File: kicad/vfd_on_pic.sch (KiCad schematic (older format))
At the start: 8 parts, among them J1 ICSP Header, J2 I2C and Power, J3 Elements, J4 Grid Multiplexor, U1 PIC16F18345

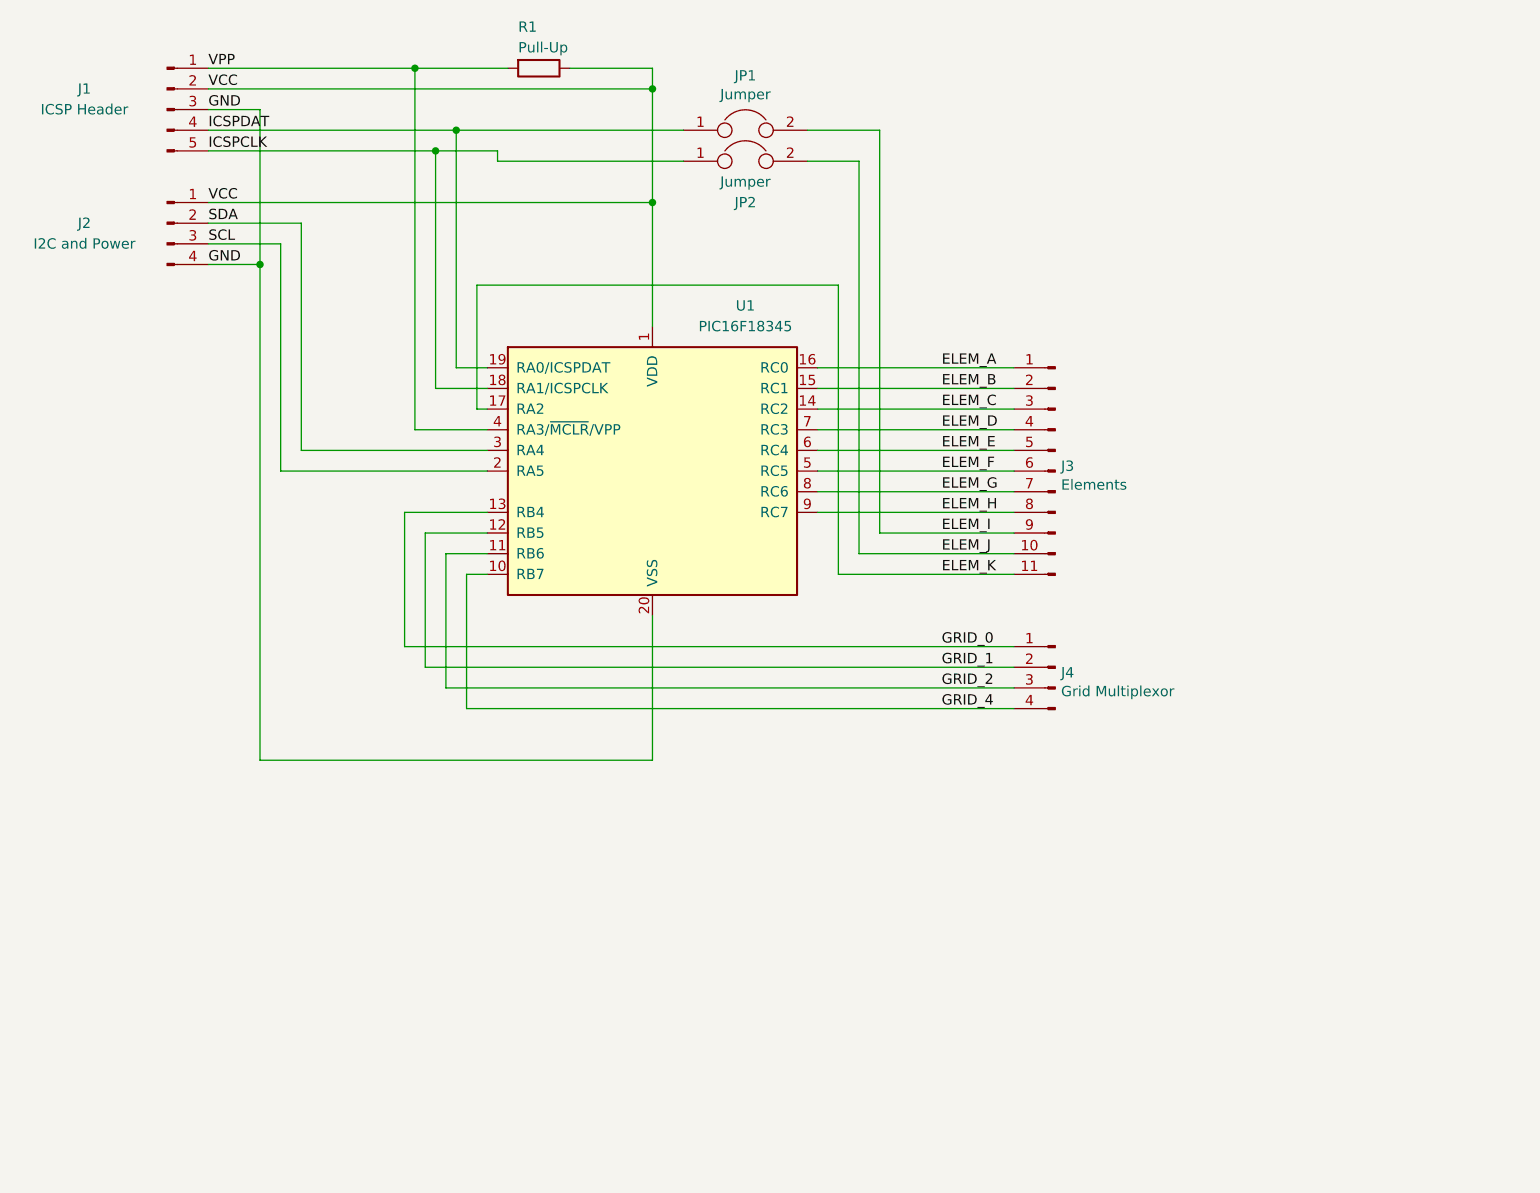
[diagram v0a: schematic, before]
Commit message: Add 74x138 3-8 decoder and uln2003 Darlington array
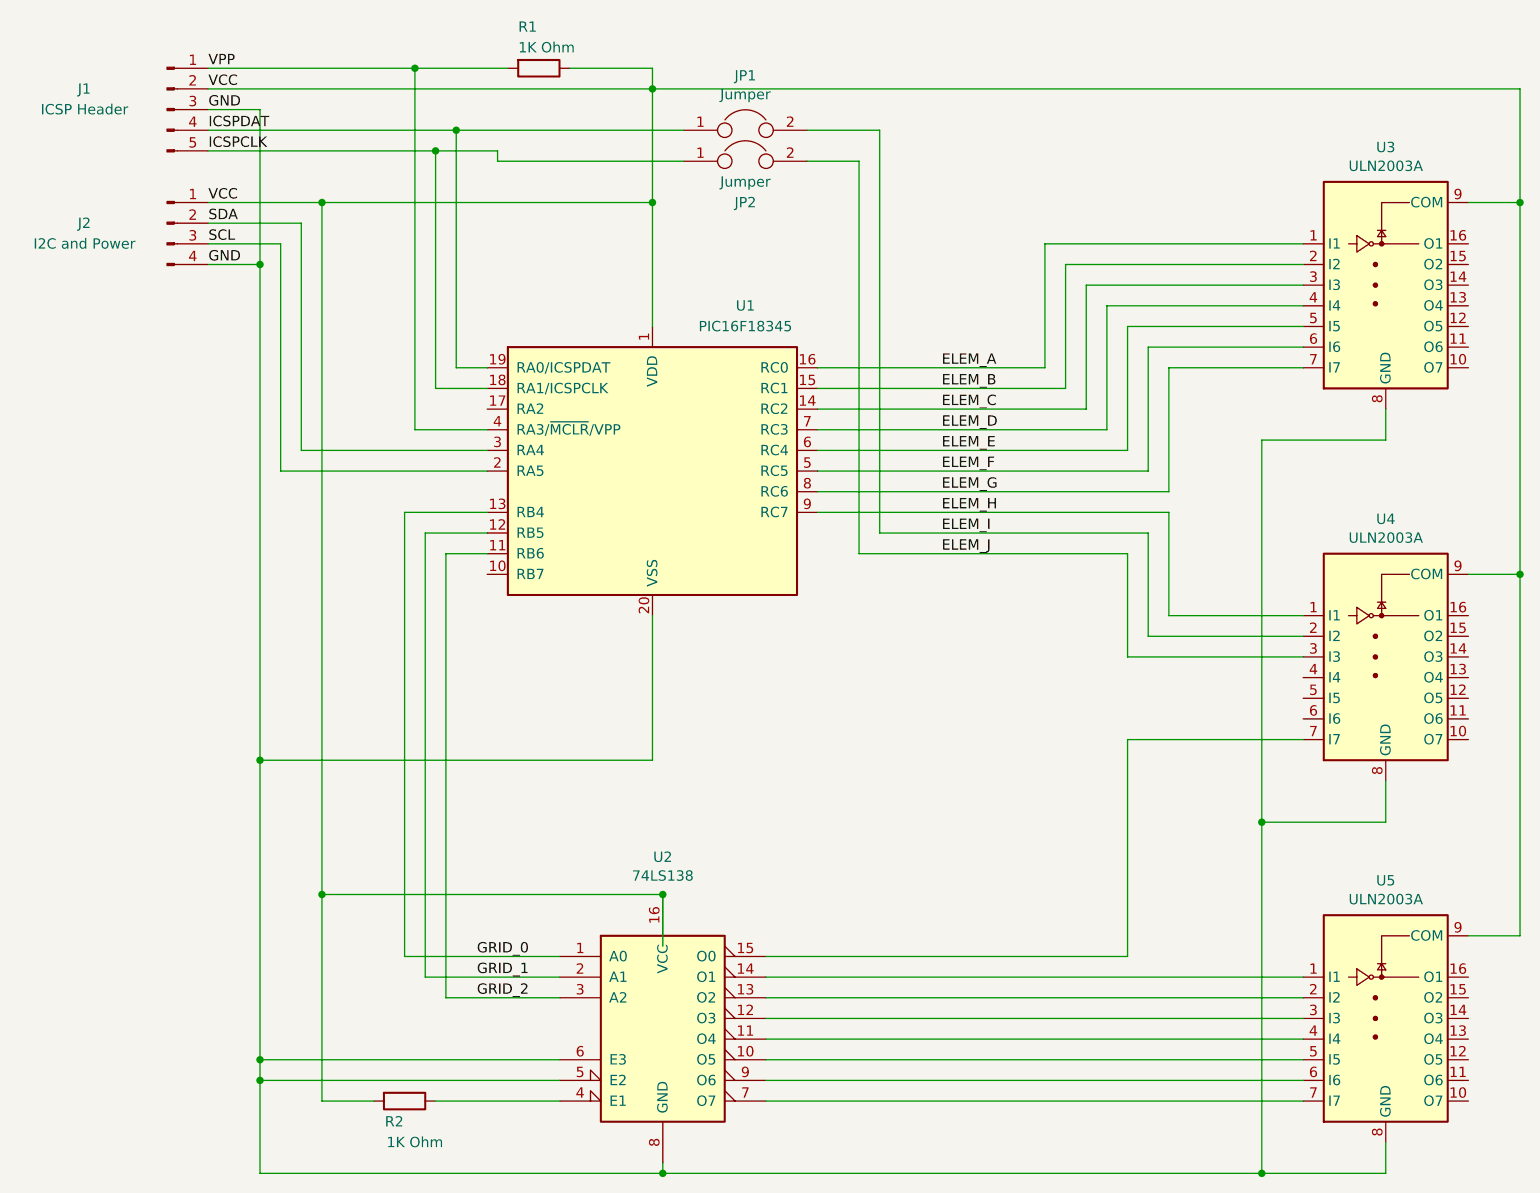
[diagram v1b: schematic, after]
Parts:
- removed J3: Elements, symbol Connector:Conn_01x11_Male
- removed J4: Grid Multiplexor, symbol Connector:Conn_01x04_Male
- added R2: 1K Ohm, symbol Device:R
- added U2: 74LS138, symbol 74xx:74LS138
- added U3, U4, U5: ULN2003A, symbol Transistor_Array:ULN2003A
- R1: value Pull-Up -> 1K Ohm
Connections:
- net ELEM_A: now also U3.1 (I1)
- net ELEM_B: now also U3.2 (I2)
- net ELEM_C: now also U3.3 (I3)
- net ELEM_D: now also U3.4 (I4)
- net ELEM_E: now also U3.5 (I5)
- net ELEM_F: now also U3.6 (I6)
- net ELEM_G: now also U3.7 (I7)
- net ELEM_H: now also U4.1 (I1)
- net ELEM_I: now also U4.2 (I2)
- net ELEM_J: now also U4.3 (I3)
- net GND: now also U2.5 (E2), U2.6 (E3), U2.8 (GND), U3.8 (GND), U4.8 (GND), U5.8 (GND)
- net GRID_0: now also U2.1 (A0)
- net GRID_1: now also U2.2 (A1)
- net GRID_2: now also U2.3 (A2)
- net VCC: now also R2.2, U2.16 (VCC), U3.9 (COM), U4.9 (COM), U5.9 (COM)
- net ELEM_K: no longer names the net of U1.17 (RA2)
- net GRID_4: no longer names the net of U1.10 (RB7)
- new net: U2.10 (O5), U5.5 (I5)
- new net: U2.11 (O4), U5.4 (I4)
- new net: U2.12 (O3), U5.3 (I3)
- new net: U2.13 (O2), U5.2 (I2)
- new net: U2.14 (O1), U5.1 (I1)
- new net: U2.15 (O0), U4.7 (I7)
- new net: R2.1, U2.4 (E1)
- new net: U2.7 (O7), U5.7 (I7)
- new net: U2.9 (O6), U5.6 (I6)
